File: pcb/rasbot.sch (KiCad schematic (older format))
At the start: 0 parts

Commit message: Fix Merges
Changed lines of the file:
@@
 EESchema Schematic File Version 4
 LIBS:rasbot-cache
-LIBS:inter-cache
 EELAYER 29 0
 EELAYER END
@@
 $EndDescr
 $Sheet
-S 4850 1250 1400 1700
+S 4550 2850 1400 1700
 U 5D0ADCD4
 F0 "MCU" 50
 F1 "mcu.sch" 50
-F2 "IR_SEL" I R 6250 1350 50
-F3 "IR_OUT" I R 6250 1450 50
-F4 "IR_EN" I R 6250 1550 50
+F2 "IR_SEL" I R 5950 2950 50
+F3 "IR_OUT" I R 5950 3050 50
+F4 "IR_EN" I R 5950 3150 50
 $EndSheet
 $Sheet
@@
 F1 "motors.sch" 50
 $EndSheet
-Text Label 6250 1350 0    50   ~ 0
+Text Label 5950 2950 0    50   ~ 0
 IR_SEL
 Text Label 9200 1300 2    50   ~ 0
@@
 Text Label 9200 1400 2    50   ~ 0
 IR_OUT
-Text Label 6250 1450 0    50   ~ 0
+Text Label 5950 3050 0    50   ~ 0
 IR_OUT
 Text Label 9200 1500 2    50   ~ 0
 IR_EN
-Text Label 6250 1550 0    50   ~ 0
+Text Label 5950 3150 0    50   ~ 0
 IR_EN
 $Sheet

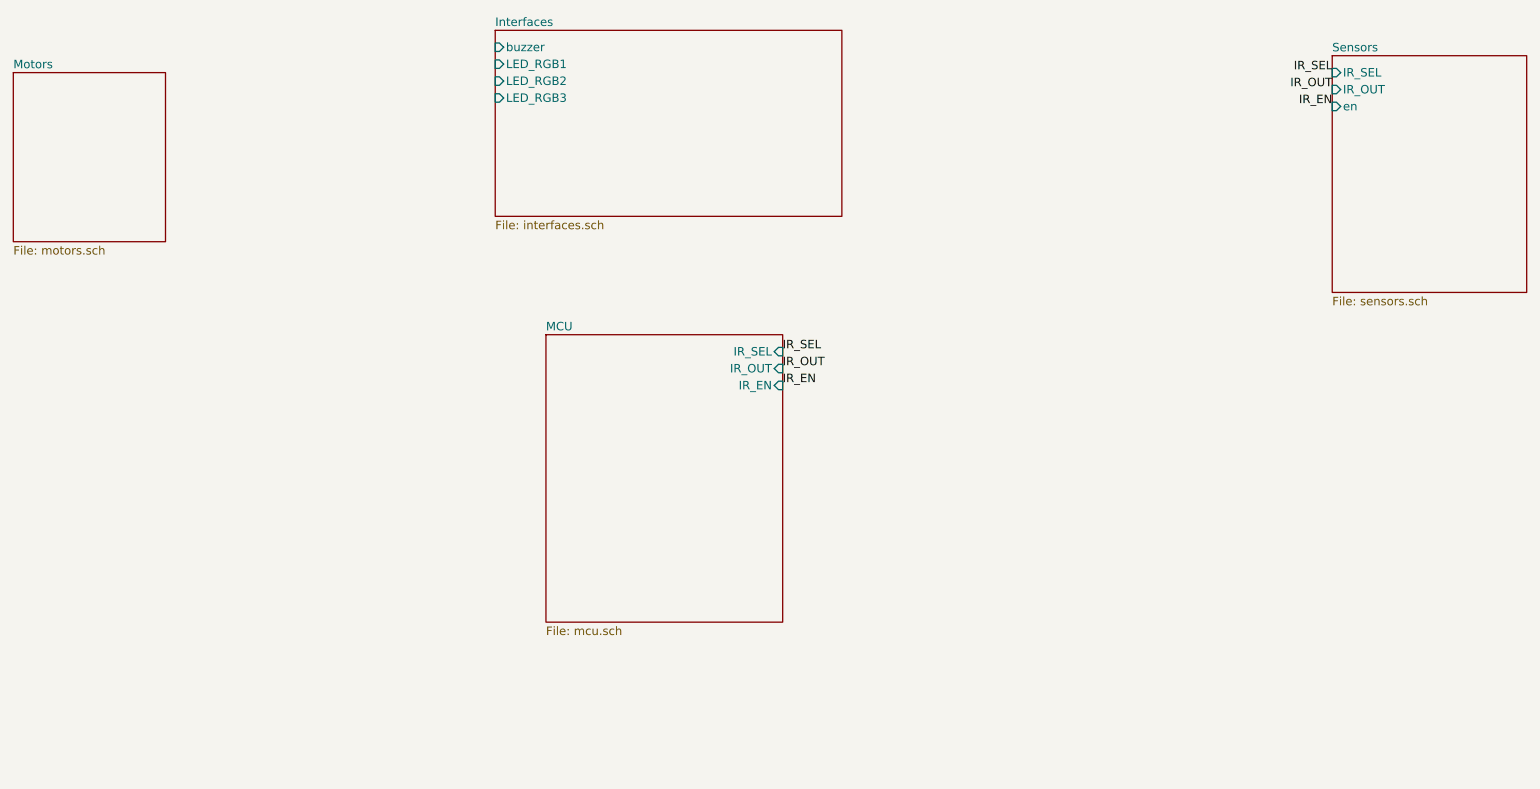
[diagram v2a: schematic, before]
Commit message: MCU connections, OLED and Sonar
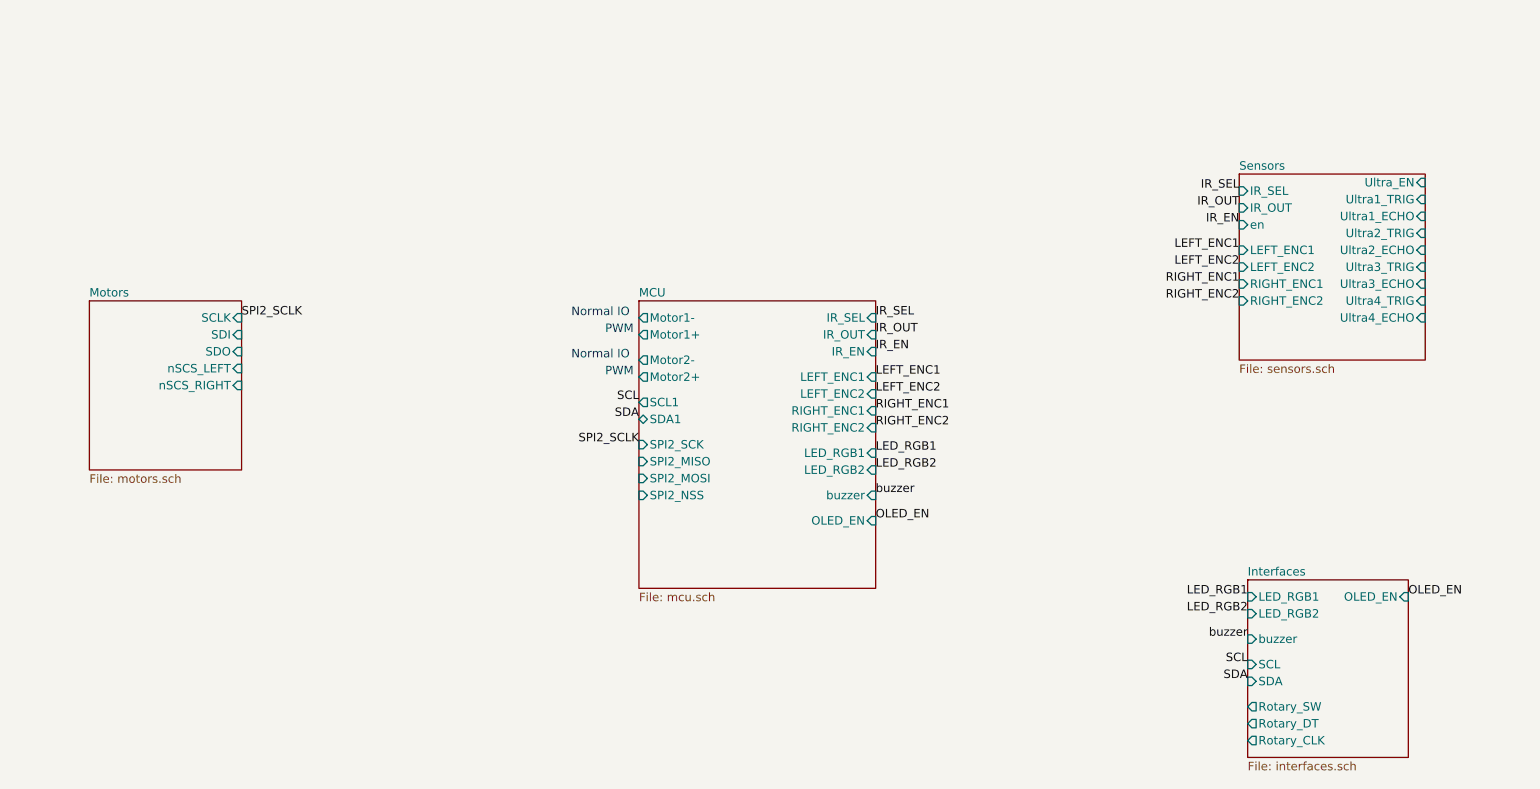
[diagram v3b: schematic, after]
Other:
- note added: "Normal IO"
- note added: "PWM"
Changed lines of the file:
@@
 $EndDescr
 $Sheet
-S 4550 2850 1400 1700
+S 5100 2650 1400 1700
 U 5D0ADCD4
 F0 "MCU" 50
 F1 "mcu.sch" 50
-F2 "IR_SEL" I R 5950 2950 50
-F3 "IR_OUT" I R 5950 3050 50
-F4 "IR_EN" I R 5950 3150 50
+F2 "IR_SEL" I R 6500 2750 50
+F3 "IR_OUT" I R 6500 2850 50
+F4 "IR_EN" I R 6500 2950 50
+F5 "LEFT_ENC1" I R 6500 3100 50
+F6 "LEFT_ENC2" I R 6500 3200 50
+F7 "RIGHT_ENC1" I R 6500 3300 50
+F8 "RIGHT_ENC2" I R 6500 3400 50
+F9 "LED_RGB1" I R 6500 3550 50
+F10 "SPI2_SCK" I L 5100 3500 50
+F11 "SPI2_NSS" I L 5100 3800 50
+F12 "SPI2_MISO" I L 5100 3600 50
+F13 "SPI2_MOSI" I L 5100 3700 50
+F14 "LED_RGB2" I R 6500 3650 50
+F15 "buzzer" I R 6500 3800 50
+F16 "OLED_EN" I R 6500 3950 50
+F17 "Motor2+" O L 5100 3100 50
+F18 "Motor2-" O L 5100 3000 50
+F19 "Motor1-" O L 5100 2750 50
+F20 "Motor1+" O L 5100 2850 50
+F21 "SCL1" O L 5100 3250 50
+F22 "SDA1" B L 5100 3350 50
 $EndSheet
 $Sheet
-S 9200 1200 1150 1400
+S 8650 1900 1100 1100
 U 5D1373A3
 F0 "Sensors" 50
 F1 "sensors.sch" 50
-F2 "IR_SEL" I L 9200 1300 50
-F3 "IR_OUT" I L 9200 1400 50
-F4 "en" I L 9200 1500 50
+F2 "IR_SEL" I L 8650 2000 50
+F3 "IR_OUT" I L 8650 2100 50
+F4 "en" I L 8650 2200 50
+F5 "LEFT_ENC1" I L 8650 2350 50
+F6 "LEFT_ENC2" I L 8650 2450 50
+F7 "RIGHT_ENC1" I L 8650 2550 50
+F8 "RIGHT_ENC2" I L 8650 2650 50
+F9 "Ultra3_TRIG" I R 9750 2450 50
+F10 "Ultra3_ECHO" I R 9750 2550 50
+F11 "Ultra_EN" I R 9750 1950 50
+F12 "Ultra2_TRIG" I R 9750 2250 50
+F13 "Ultra2_ECHO" I R 9750 2350 50
+F14 "Ultra1_TRIG" I R 9750 2050 50
+F15 "Ultra1_ECHO" I R 9750 2150 50
+F16 "Ultra4_TRIG" I R 9750 2650 50
+F17 "Ultra4_ECHO" I R 9750 2750 50
 $EndSheet
 $Sheet
-S 1400 1300 900  1000
+S 1850 2650 900  1000
 U 5D25A1F3
 F0 "Motors" 50
 F1 "motors.sch" 50
+F2 "SCLK" I R 2750 2750 50
+F3 "SDI" I R 2750 2850 50
+F4 "SDO" I R 2750 2950 50
+F5 "nSCS_LEFT" I R 2750 3050 50
+F6 "nSCS_RIGHT" I R 2750 3150 50
 $EndSheet
-Text Label 5950 2950 0    50   ~ 0
+Text Label 6500 2750 0    50   ~ 0
 IR_SEL
-Text Label 9200 1300 2    50   ~ 0
+Text Label 8650 2000 2    50   ~ 0
 IR_SEL
-Text Label 9200 1400 2    50   ~ 0
+Text Label 8650 2100 2    50   ~ 0
 IR_OUT
-Text Label 5950 3050 0    50   ~ 0
+Text Label 6500 2850 0    50   ~ 0
 IR_OUT
-Text Label 9200 1500 2    50   ~ 0
+Text Label 8650 2200 2    50   ~ 0
 IR_EN
-Text Label 5950 3150 0    50   ~ 0
+Text Label 6500 2950 0    50   ~ 0
 IR_EN
 $Sheet
-S 4250 1050 2050 1100
+S 8700 4300 950  1050
 U 5D3A4E48
 F0 "Interfaces" 50
 F1 "interfaces.sch" 50
-F2 "buzzer" I L 4250 1150 50
-F3 "LED_RGB1" I L 4250 1250 50
-F4 "LED_RGB3" I L 4250 1450 50
-F5 "LED_RGB2" I L 4250 1350 50
+F2 "buzzer" I L 8700 4650 50
+F3 "LED_RGB1" I L 8700 4400 50
+F4 "LED_RGB2" I L 8700 4500 50
+F5 "SDA" I L 8700 4900 50
+F6 "Rotary_SW" O L 8700 5050 50
+F7 "Rotary_DT" O L 8700 5150 50
+F8 "Rotary_CLK" O L 8700 5250 50
+F9 "SCL" I L 8700 4800 50
+F10 "OLED_EN" I R 9650 4400 50
 $EndSheet
+Text Notes 4700 2750 0    50   ~ 0
+Normal IO
+Text Notes 4900 2850 0    50   ~ 0
+PWM
+Text Notes 4700 3000 0    50   ~ 0
+Normal IO
+Text Notes 4900 3100 0    50   ~ 0
+PWM
+Text Label 6500 3100 0    50   ~ 0
+LEFT_ENC1
+Text Label 6500 3400 0    50   ~ 0
+RIGHT_ENC2
+Text Label 6500 3200 0    50   ~ 0
+LEFT_ENC2
+Text Label 6500 3300 0    50   ~ 0
+RIGHT_ENC1
+Text Label 8650 2350 2    50   ~ 0
+LEFT_ENC1
+Text Label 8650 2650 2    50   ~ 0
+RIGHT_ENC2
+Text Label 8650 2450 2    50   ~ 0
+LEFT_ENC2
+Text Label 8650 2550 2    50   ~ 0
+RIGHT_ENC1
+Text Label 6500 3550 0    50   ~ 0
+LED_RGB1
+Text Label 6500 3650 0    50   ~ 0
+LED_RGB2
+Text Label 6500 3800 0    50   ~ 0
+buzzer
+Text Label 8700 4400 2    50   ~ 0
+LED_RGB1
+Text Label 8700 4500 2    50   ~ 0
+LED_RGB2
+Text Label 8700 4650 2    50   ~ 0
+buzzer
+Text Label 5100 3500 2    50   ~ 0
+SPI2_SCLK
+Text Label 2750 2750 0    50   ~ 0
+SPI2_SCLK
+Text Label 8700 4800 2    50   ~ 0
+SCL
+Text Label 8700 4900 2    50   ~ 0
+SDA
+Text Label 5100 3250 2    50   ~ 0
+SCL
+Text Label 5100 3350 2    50   ~ 0
+SDA
+Text Label 9650 4400 0    50   ~ 0
+OLED_EN
+Text Label 6500 3950 0    50   ~ 0
+OLED_EN
 $EndSCHEMATC

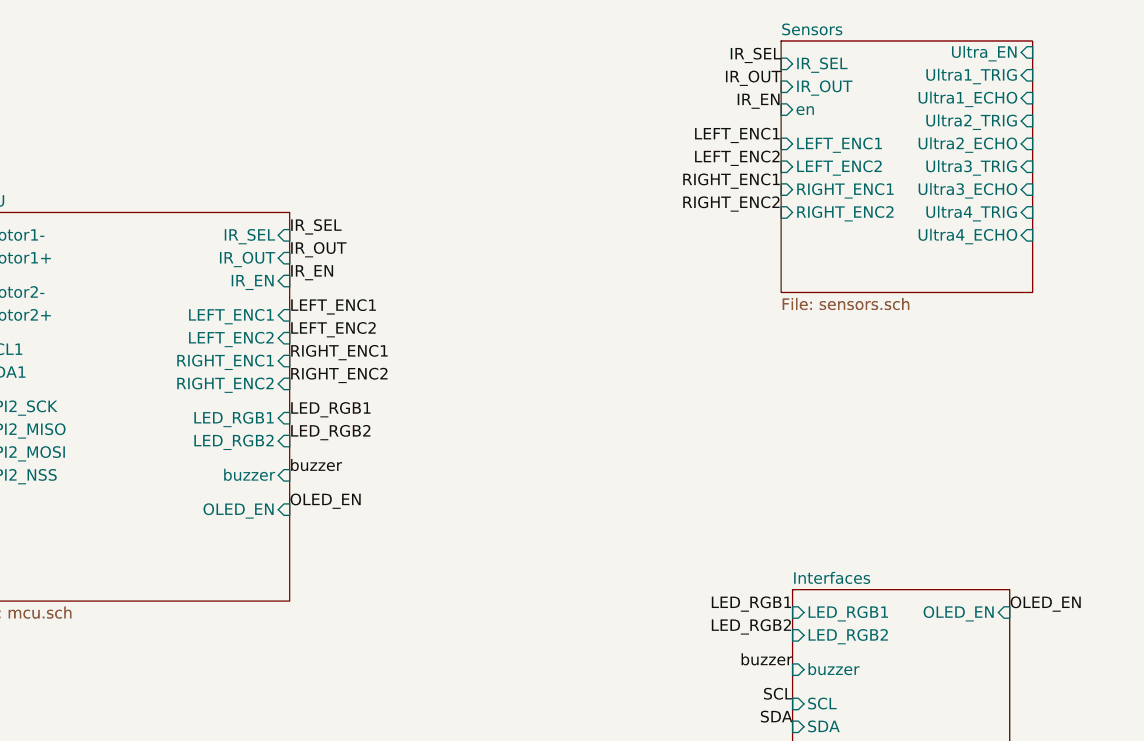
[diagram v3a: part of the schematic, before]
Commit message: Connect Ultrasonic Sensors
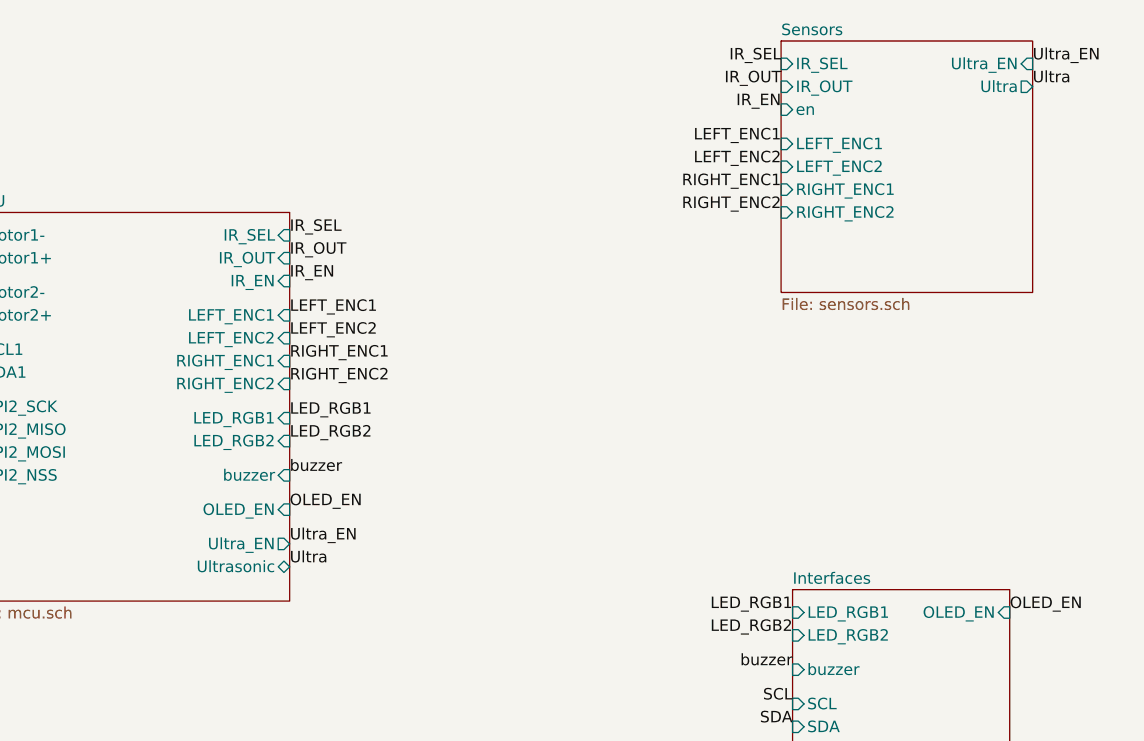
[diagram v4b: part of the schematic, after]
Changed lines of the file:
@@
 F21 "SCL1" O L 5100 3250 50
 F22 "SDA1" B L 5100 3350 50
+F23 "Ultrasonic" B R 6500 4200 50
+F24 "Ultra_EN" O R 6500 4100 50
 $EndSheet
 $Sheet
@@
 F7 "RIGHT_ENC1" I L 8650 2550 50
 F8 "RIGHT_ENC2" I L 8650 2650 50
-F9 "Ultra3_TRIG" I R 9750 2450 50
-F10 "Ultra3_ECHO" I R 9750 2550 50
-F11 "Ultra_EN" I R 9750 1950 50
-F12 "Ultra2_TRIG" I R 9750 2250 50
-F13 "Ultra2_ECHO" I R 9750 2350 50
-F14 "Ultra1_TRIG" I R 9750 2050 50
-F15 "Ultra1_ECHO" I R 9750 2150 50
-F16 "Ultra4_TRIG" I R 9750 2650 50
-F17 "Ultra4_ECHO" I R 9750 2750 50
+F9 "Ultra_EN" I R 9750 2000 50
+F10 "Ultra" O R 9750 2100 50
 $EndSheet
 $Sheet
@@
 Text Label 6500 3950 0    50   ~ 0
 OLED_EN
+Text Label 9750 2100 0    50   ~ 0
+Ultra
+Text Label 9750 2000 0    50   ~ 0
+Ultra_EN
+Text Label 6500 4200 0    50   ~ 0
+Ultra
+Text Label 6500 4100 0    50   ~ 0
+Ultra_EN
 $EndSCHEMATC

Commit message: Rotary Encoder
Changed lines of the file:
@@
 F23 "Ultrasonic" B R 6500 4200 50
 F24 "Ultra_EN" O R 6500 4100 50
+F25 "Rotary_DT" I L 5100 4050 50
+F26 "Rotary_CLK" I L 5100 4150 50
+F27 "Rotary_SW" I L 5100 3950 50
 $EndSheet
 $Sheet
@@
 Text Label 6500 4100 0    50   ~ 0
 Ultra_EN
+Text Label 8700 5050 2    50   ~ 0
+Rotary_SW
+Text Label 8700 5150 2    50   ~ 0
+Rotary_DT
+Text Label 8700 5250 2    50   ~ 0
+Rotary_CLK
+Text Label 5100 3950 2    50   ~ 0
+Rotary_SW
+Text Label 5100 4050 2    50   ~ 0
+Rotary_DT
+Text Label 5100 4150 2    50   ~ 0
+Rotary_CLK
 $EndSCHEMATC
